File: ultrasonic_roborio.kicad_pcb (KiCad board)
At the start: 2 copper layers, 50.8 x 33 mm, 16 parts, among them J1 PCM solenoid, J2 Sensor0, J3 roboRIO A0, J4 Sensor1, J5 roboRIO A1, SW0 SW_Push, SW1 SW_Push, SW2 SW_Push, SW3 SW_Push

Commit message: Add 3D models of Weidmüller terminal blocks This required renaming the footprint libraries to not have spaces. The spaces were invalid characters, but not validated until I opened the footprint properties dialog.
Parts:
- J1: footprint ultrasonic_roborio:LSF-SMT 3.50_02_135 3.5SN -> ultrasonic_roborio:LSF-SMT_3.50_02_135_3.5SN
- J2, J4: footprint ultrasonic_roborio:LSF-SMT 3.50_04_135 3.5SN -> ultrasonic_roborio:LSF-SMT_3.50_04_135_3.5SN

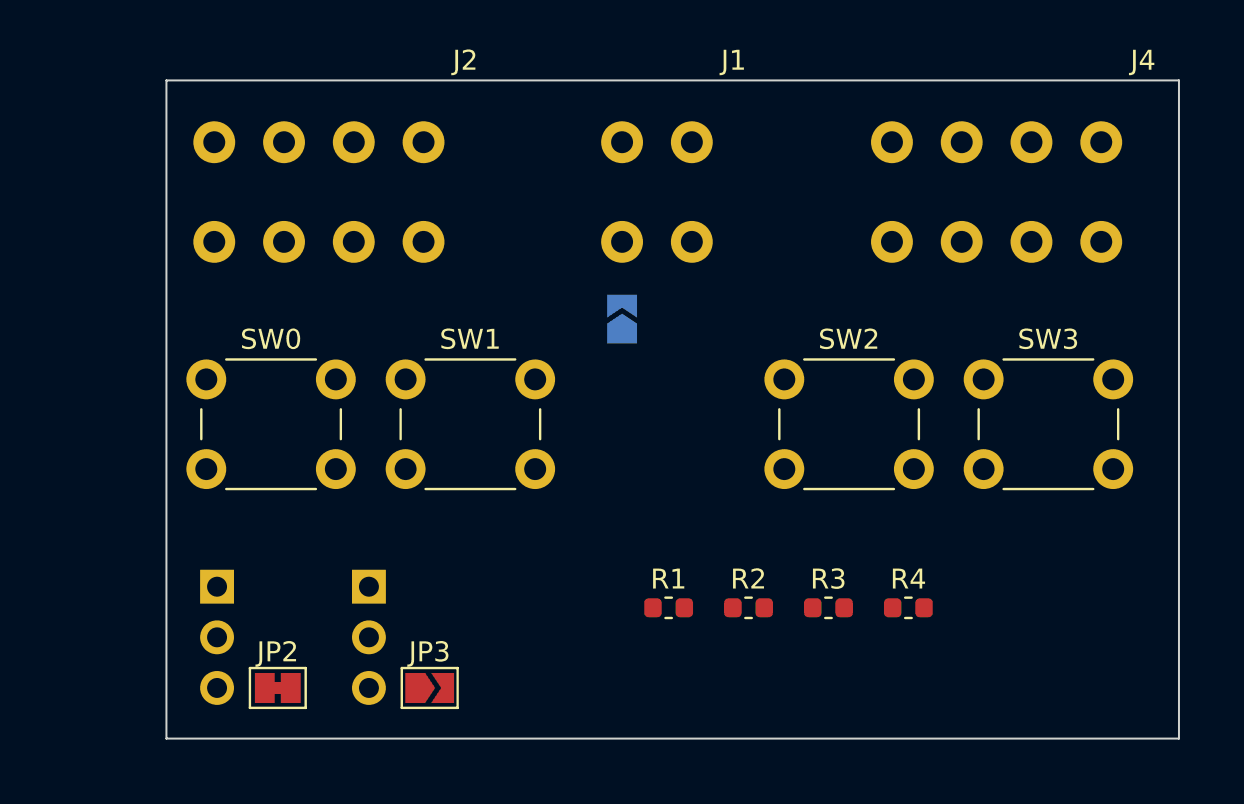
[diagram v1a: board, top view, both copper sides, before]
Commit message: Switch to smaller switches
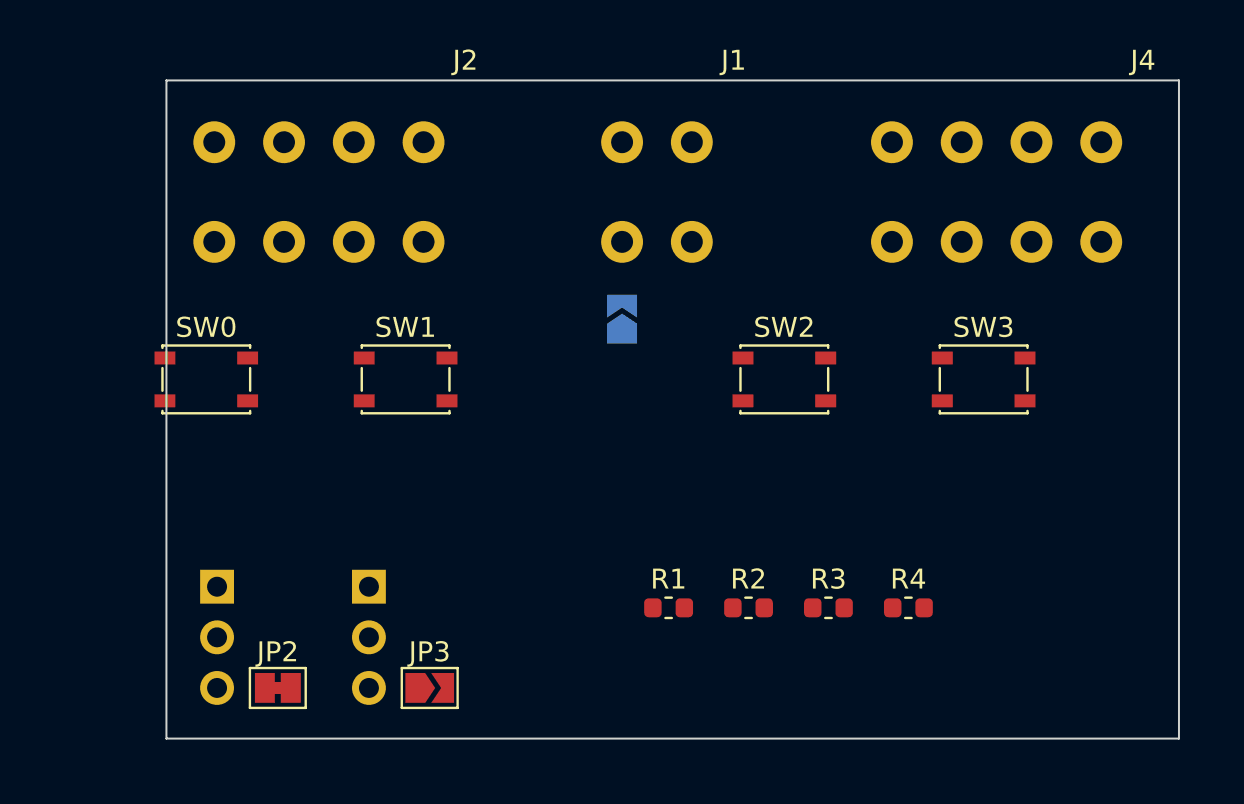
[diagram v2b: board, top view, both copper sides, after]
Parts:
- SW0, SW1, SW2, SW3: footprint Button_Switch_THT:SW_PUSH_6mm -> Button_Switch_SMD:SW_SPST_PTS810

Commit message: Initial work on tracing
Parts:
- moved R1 25.2 mm to (78.7, 91.6), turned to 90 degrees
- moved R2 24.4 mm to (82.4, 94.5), turned to 270 degrees
- moved SW1 20.1 mm to (97.5, 96.5)
- moved R3 12.7 mm to (119.9, 95.5), turned to 90 degrees
- moved R4 11.1 mm to (124.3, 100.8), turned to 270 degrees
- moved SW3 6.32 mm to (113.8, 96.5)
- moved JP1 6.27 mm to (94.1, 84.3), turned to 180 degrees
- moved SW2 5.54 mm to (105.7, 96.5)
- moved SW0 5.46 mm to (89.4, 96.5)
- moved JP2 0.76 mm to (82.5, 106.7)
- moved J2 0.11 mm to (91.3, 76.2)
- renumbered SW1 to SW0, SW0 to SW1
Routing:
- net /Out1: track 0.00 -> 45.8 mm
- net +24V: track 0.00 -> 33.3 mm
- net /Teach0: track 0.00 -> 24.1 mm
- net /Teach1: track 0.00 -> 24.0 mm
- net GND: track 0.00 -> 22.8 mm, vias 0 -> 7
- net /SensorOut1: track 0.00 -> 13.4 mm
- net /Out0: track 0.00 -> 12.9 mm
- net /SensorOut0: track 0.00 -> 6.49 mm
- net Net-(J1-Pad2): track 0.00 -> 4.24 mm
- net Net-(J3-Pad3): track 0.00 -> 3.16 mm
- net Net-(J5-Pad3): track 0.00 -> 2.32 mm
- added copper zone on B.Cu, net GND

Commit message: Finish routing; adjustments to placement
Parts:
- moved R4 40.2 mm to (84.3, 96.8), turned to 90 degrees
- moved R3 33.6 mm to (86.4, 96.8)
- moved SW3 15.2 mm to (98.6, 96.0)
- moved SW2 8.45 mm to (98.6, 91.9), turned to 180 degrees
- moved SW1 6.12 mm to (91.4, 96.0)
- moved R1 5.21 mm to (78.7, 96.8)
- moved SW0 5.00 mm to (91.4, 91.9), turned to 180 degrees
- moved R2 2.82 mm to (80.8, 96.8), turned to 90 degrees
- moved JP3 0.72 mm to (90.1, 106.7)
- moved JP1 0.22 mm to (94.3, 84.3)
- moved JP2 0.13 mm to (82.4, 106.7)
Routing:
- net /Out1: track 45.8 -> 5.54 mm
- net +24V: track 33.3 -> 63.6 mm
- net /SensorOut1: track 13.4 -> 36.6 mm
- net /Teach1: track 24.0 -> 39.7 mm
- net /SensorOut0: track 6.49 -> 16.8 mm
- net /Out0: track 12.9 -> 6.05 mm
- net Net-(J1-Pad2): track 4.24 -> 9.52 mm
- net /Teach0: track 24.1 -> 25.1 mm
- net Net-(J5-Pad3): track 2.32 -> 3.05 mm
- net GND: track 22.8 -> 22.1 mm, vias 7 -> 6

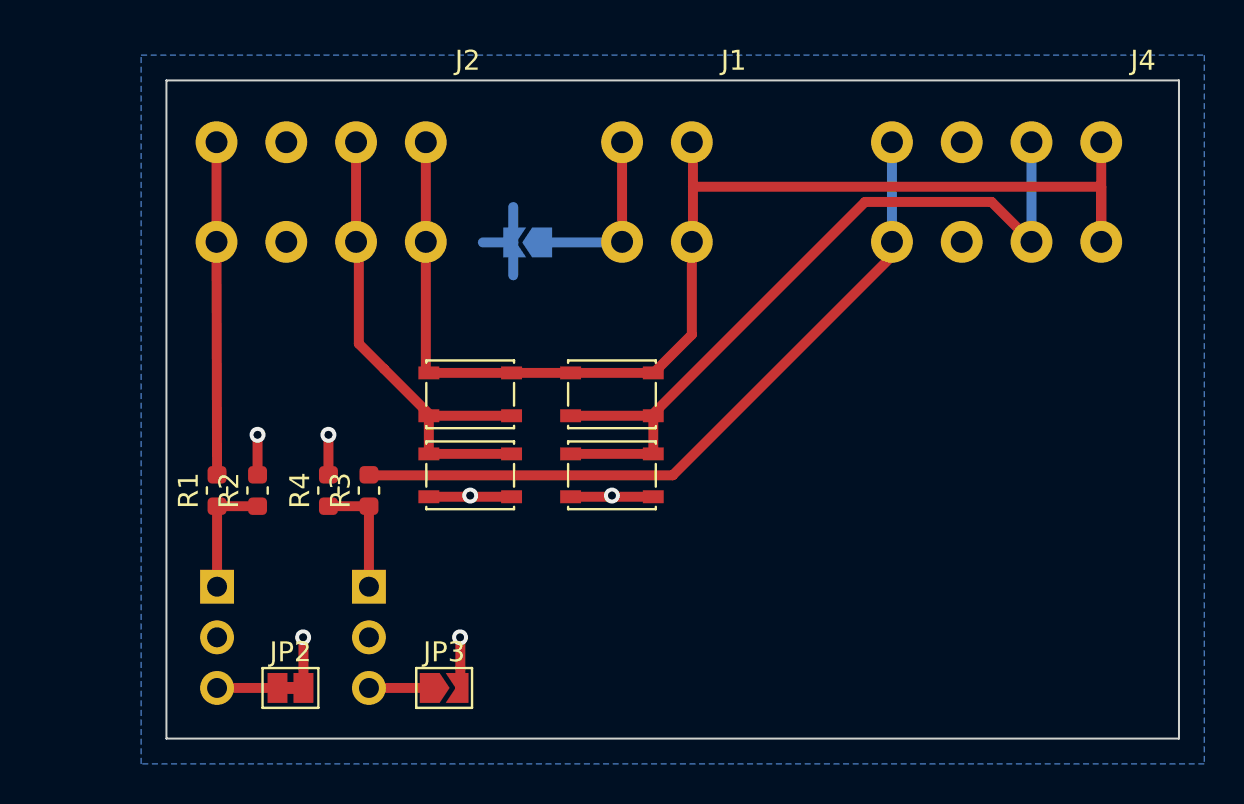
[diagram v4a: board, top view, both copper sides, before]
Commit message: Finish v0 PCB design Add protection resistor for if A1 and A2 pressed at the same time Change layout to reduce board size Move buttons to not have wires running over them (risk of accidential triggering) Add author names This commit has the gerbers that were ordered as the ZIP file
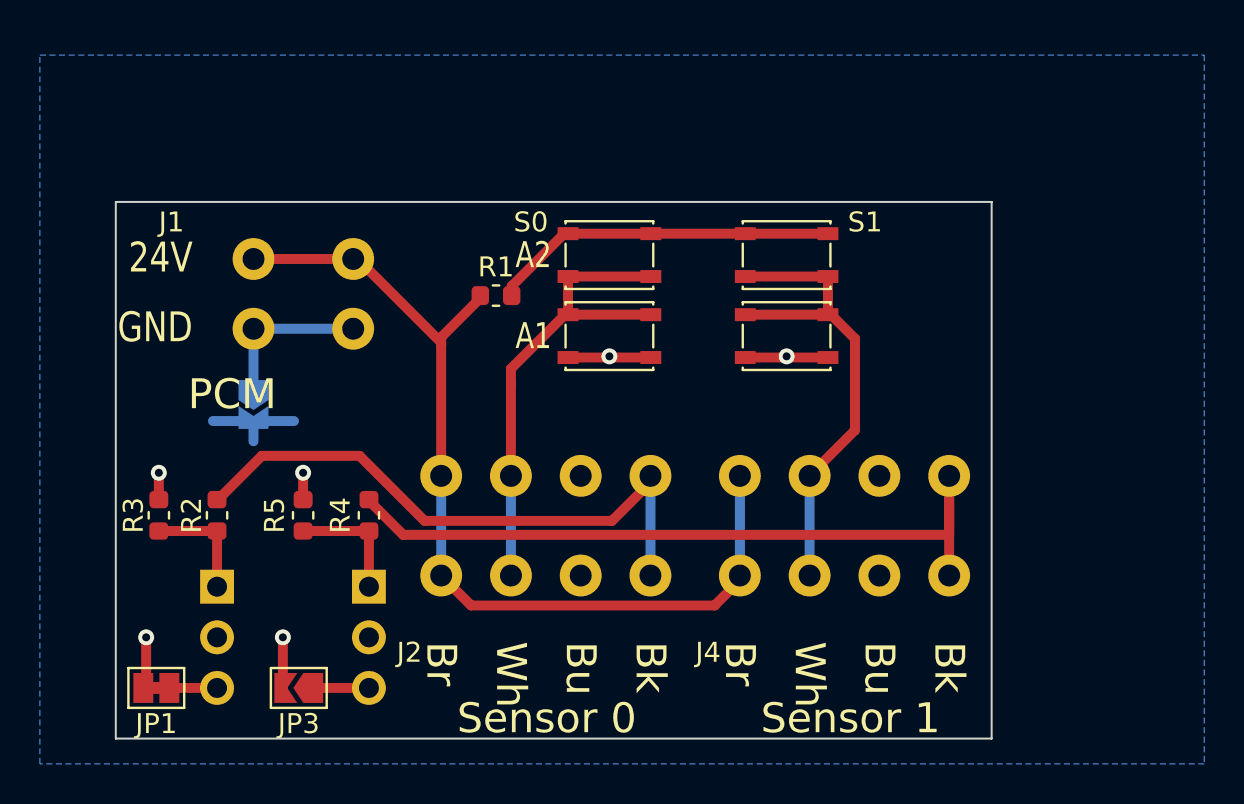
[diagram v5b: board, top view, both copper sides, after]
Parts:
- removed the JP1 at (94.3, 84.3)
- removed SW0: SW_Push, Button_Switch_SMD:SW_SPST_PTS810
- added JP2: SolderJumper_2_Open, Jumper:SolderJumper-2_P1.3mm_Open_TrianglePad1.0x1.5mm, B.Cu at (80.6, 92.5)
- added R5: 4.7k, Resistor_SMD:R_0603_1608Metric, F.Cu at (83.1, 98.0)
- added SW4: SW_Push, Button_Switch_SMD:SW_SPST_PTS810, F.Cu at (107.3, 89.0)
- R1: value 4.7k -> 330
- moved J4 35.8 mm to (102.9, 104.1), turned to 0 degrees
- moved J2 28.1 mm to (87.9, 104.1), turned to 0 degrees
- moved J1 28.0 mm to (77.5, 83.1), turned to 270 degrees
- moved R1 17.1 mm to (92.7, 87.0), turned to 0 degrees
- moved SW3 14.1 mm to (107.3, 85.0), turned to 180 degrees
- moved SW1 13.1 mm to (98.4, 85.0), turned to 180 degrees
- moved R3 10.6 mm to (75.8, 98.0)
- moved JP3 7.29 mm to (82.8, 106.7), turned to 180 degrees
- moved JP1 6.73 mm to (75.7, 106.7), turned to 180 degrees
- moved SW2 2.92 mm to (98.4, 89.0), turned to 0 degrees
- moved R2 2.38 mm to (78.7, 98.0)
- moved R4 2.38 mm to (86.4, 98.0)
- renumbered JP2 to JP1
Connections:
- R1 pad 1: /Out0 -> +24V
- R1 pad 2: /SensorOut0 -> /TeachV+
- R2 pad 2: GND -> /SensorOut0
- R3 pad 1: /Out1 -> /Out0
- R3 pad 2: /SensorOut1 -> GND
- R4 pad 2: GND -> /SensorOut1
- SW1 pad 2: GND -> /TeachV+
- SW2 pad 1: /Teach1 -> /Teach0
- SW2 pad 2: +24V -> GND
- SW3 pad 2: GND -> /TeachV+
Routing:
- net /TeachV+: track 0.00 -> 17.7 mm
- net +24V: track 63.6 -> 47.7 mm
- net /Teach1: track 39.7 -> 24.7 mm
- net /SensorOut0: track 16.8 -> 30.1 mm
- net GND: track 22.1 -> 20.8 mm
- net /SensorOut1: track 36.6 -> 38.0 mm
- net Net-(J1-Pad2): track 9.52 -> 8.43 mm
- net Net-(J3-Pad3): track 3.16 -> 2.29 mm
- net /Teach0: track 25.1 -> 24.6 mm
- net /Out1: track 5.54 -> 6.10 mm
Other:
- board size 50.8 x 33 mm -> 43.9 x 26.9 mm
- rule pad_to_mask_clearance: 0.051 -> 0.0508
- rule solder_mask_min_width: 0.25 -> 0.1016
- rule trace_min: 0.2 -> 0.1524
- rule via_min_drill: 0.3 -> 0.254
- rule via_min_size: 0.4 -> 0.508
- board text added: "24V"
- board text added: "A1"
- board text added: "A2"
- board text added: "Bk"
- board text added: "Br"
- board text added: "Bu"
- board text added: "GND"
- board text added: "PCM"
- board text added: "S0"
- board text added: "S1"
- board text added: "Sean Tierney, Schuyler St. Leger Team Caution Robotics #1492"
- board text added: "Sensor 0"
- board text added: "Sensor 1"
- board text added: "Wh"
- board text added: "ultrasonic_roborio v0 2020"
